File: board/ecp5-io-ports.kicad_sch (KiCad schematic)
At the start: 9 parts

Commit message: Complete schematic
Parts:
- FPGA1: value LFE5UM-381 -> LFE5U-25F; symbol FPGA_Lattice:LFE5UM-85F-6BG381x -> FPGA_Lattice:LFE5U-85F-8BG381x; JLC (none) -> CABGA-381; LCSC (none) -> C1550939
- renumbered C43 to C37, C44 to C38, C45 to C39, C46 to C40, C47 to C41, C48 to C42, C49 to C43, C50 to C44
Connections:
- no-connect marks 127 -> 131
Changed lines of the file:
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@@
 	)
 	(no_connect
+		(at 162.56 120.65)
+	)
+	(no_connect
 		(at 116.84 49.53)
 	)
@@
 	)
 	(no_connect
+		(at 162.56 105.41)
+	)
+	(no_connect
 		(at 67.31 54.61)
 	)
@@
 	)
 	(no_connect
+		(at 162.56 118.11)
+	)
+	(no_connect
 		(at 67.31 80.01)
 	)
@@
 	)
 	(no_connect
+		(at 162.56 113.03)
+	)
+	(no_connect
 		(at 22.86 49.53)
 	)
@@
 		(on_board yes)
 		(dnp no)
-		(property "Reference" "C44"
+		(property "Reference" "C38"
 			(at 65.024 148.082 0)
 			(effects
@@
 			(project "HispalisFPGA"
 				(path "/864346d0-d3ef-428e-a44f-9476f195db98/79b2db60-ab3f-4b1c-9160-e735db7b00f9"
-					(reference "C44")
+					(reference "C38")
 					(unit 1)
 				)
@@
 		(on_board yes)
 		(dnp no)
-		(property "Reference" "C49"
+		(property "Reference" "C43"
 			(at 183.134 35.052 0)
 			(effects
@@
 			(project "HispalisFPGA"
 				(path "/864346d0-d3ef-428e-a44f-9476f195db98/79b2db60-ab3f-4b1c-9160-e735db7b00f9"
-					(reference "C49")
+					(reference "C43")
 					(unit 1)
 				)
@@
 	)
 	(symbol
-		(lib_id "FPGA_Lattice:LFE5UM-85F-6BG381x")
+		(lib_id "FPGA_Lattice:LFE5U-85F-8BG381x")
 		(at 77.47 82.55 0)
 		(unit 3)
@@
 			)
 		)
-		(property "Value" "LFE5UM-381"
+		(property "Value" "LFE5U-25F"
 			(at 83.82 83.8199 0)
 			(effects
@@
 			)
 		)
-		(property "Description" "ECP5 FPGA, 84K LUTs, 1.2V, 3.2Gbps SERDES, BGA-381"
+		(property "Description" "ECP5 FPGA, 84K LUTs, 1.2V, BGA-381"
+			(at 77.47 82.55 0)
+			(effects
+				(font
+					(size 1.27 1.27)
+				)
+				(hide yes)
+			)
+		)
+		(property "JLC" "CABGA-381"
+			(at 77.47 82.55 0)
+			(effects
+				(font
+					(size 1.27 1.27)
+				)
+				(hide yes)
+			)
+		)
+		(property "LCSC" "C1550939"
 			(at 77.47 82.55 0)
 			(effects
@@
 	)
 	(symbol
-		(lib_id "FPGA_Lattice:LFE5UM-85F-6BG381x")
+		(lib_id "FPGA_Lattice:LFE5U-85F-8BG381x")
 		(at 92.71 193.04 0)
 		(unit 7)
@@
 			)
 		)
-		(property "Value" "LFE5UM-381"
+		(property "Value" "LFE5U-25F"
 			(at 99.06 194.3099 0)
 			(effects
@@
 			)
 		)
-		(property "Description" "ECP5 FPGA, 84K LUTs, 1.2V, 3.2Gbps SERDES, BGA-381"
+		(property "Description" "ECP5 FPGA, 84K LUTs, 1.2V, BGA-381"
+			(at 92.71 193.04 0)
+			(effects
+				(font
+					(size 1.27 1.27)
+				)
+				(hide yes)
+			)
+		)
+		(property "JLC" "CABGA-381"
+			(at 92.71 193.04 0)
+			(effects
+				(font
+					(size 1.27 1.27)
+				)
+				(hide yes)
+			)
+		)
+		(property "LCSC" "C1550939"
 			(at 92.71 193.04 0)
 			(effects
@@
 	)
 	(symbol
-		(lib_id "FPGA_Lattice:LFE5UM-85F-6BG381x")
+		(lib_id "FPGA_Lattice:LFE5U-85F-8BG381x")
 		(at 46.99 195.58 0)
 		(unit 6)
@@
 			)
 		)
-		(property "Value" "LFE5UM-381"
+		(property "Value" "LFE5U-25F"
 			(at 53.34 196.8499 0)
 			(effects
@@
 			)
 		)
-		(property "Description" "ECP5 FPGA, 84K LUTs, 1.2V, 3.2Gbps SERDES, BGA-381"
+		(property "Description" "ECP5 FPGA, 84K LUTs, 1.2V, BGA-381"
+			(at 46.99 195.58 0)
+			(effects
+				(font
+					(size 1.27 1.27)
+				)
+				(hide yes)
+			)
+		)
+		(property "JLC" "CABGA-381"
+			(at 46.99 195.58 0)
+			(effects
+				(font
+					(size 1.27 1.27)
+				)
+				(hide yes)
+			)
+		)
+		(property "LCSC" "C1550939"
 			(at 46.99 195.58 0)
 			(effects
@@
 		(on_board yes)
 		(dnp no)
-		(property "Reference" "C43"
+		(property "Reference" "C37"
 			(at 57.404 148.082 0)
 			(effects
@@
 			(project "HispalisFPGA"
 				(path "/864346d0-d3ef-428e-a44f-9476f195db98/79b2db60-ab3f-4b1c-9160-e735db7b00f9"
-					(reference "C43")
+					(reference "C37")
 					(unit 1)
 				)
@@
 	)
 	(symbol
-		(lib_id "FPGA_Lattice:LFE5UM-85F-6BG381x")
+		(lib_id "FPGA_Lattice:LFE5U-85F-8BG381x")
 		(at 127 82.55 0)
 		(unit 4)
@@
 			)
 		)
-		(property "Value" "LFE5UM-381"
+		(property "Value" "LFE5U-25F"
 			(at 133.35 83.8199 0)
 			(effects
@@
 			)
 		)
-		(property "Description" "ECP5 FPGA, 84K LUTs, 1.2V, 3.2Gbps SERDES, BGA-381"
+		(property "Description" "ECP5 FPGA, 84K LUTs, 1.2V, BGA-381"
+			(at 127 82.55 0)
+			(effects
+				(font
+					(size 1.27 1.27)
+				)
+				(hide yes)
+			)
+		)
+		(property "JLC" "CABGA-381"
+			(at 127 82.55 0)
+			(effects
+				(font
+					(size 1.27 1.27)
+				)
+				(hide yes)
+			)
+		)
+		(property "LCSC" "C1550939"
 			(at 127 82.55 0)
 			(effects
@@
 		(on_board yes)
 		(dnp no)
-		(property "Reference" "C46"
+		(property "Reference" "C40"
 			(at 110.744 148.082 0)
 			(effects
@@
 			(project "HispalisFPGA"
 				(path "/864346d0-d3ef-428e-a44f-9476f195db98/79b2db60-ab3f-4b1c-9160-e735db7b00f9"
-					(reference "C46")
+					(reference "C40")
 					(unit 1)
 				)
@@
 		(on_board yes)
 		(dnp no)
-		(property "Reference" "C47"
+		(property "Reference" "C41"
 			(at 153.924 148.082 0)
 			(effects
@@
 			(project "HispalisFPGA"
 				(path "/864346d0-d3ef-428e-a44f-9476f195db98/79b2db60-ab3f-4b1c-9160-e735db7b00f9"
-					(reference "C47")
+					(reference "C41")
 					(unit 1)
 				)
@@
 		(on_board yes)
 		(dnp no)
-		(property "Reference" "C48"
+		(property "Reference" "C42"
 			(at 161.544 148.082 0)
 			(effects
@@
 			(project "HispalisFPGA"
 				(path "/864346d0-d3ef-428e-a44f-9476f195db98/79b2db60-ab3f-4b1c-9160-e735db7b00f9"
-					(reference "C48")
+					(reference "C42")
 					(unit 1)
 				)
@@
 		(on_board yes)
 		(dnp no)
-		(property "Reference" "C45"
+		(property "Reference" "C39"
 			(at 103.124 148.082 0)
 			(effects
@@
 			(project "HispalisFPGA"
 				(path "/864346d0-d3ef-428e-a44f-9476f195db98/79b2db60-ab3f-4b1c-9160-e735db7b00f9"
-					(reference "C45")
+					(reference "C39")
 					(unit 1)
 				)
@@
 	)
 	(symbol
-		(lib_id "FPGA_Lattice:LFE5UM-85F-6BG381x")
+		(lib_id "FPGA_Lattice:LFE5U-85F-8BG381x")
 		(at 33.02 74.93 0)
 		(unit 2)
@@
 			)
 		)
-		(property "Value" "LFE5UM-381"
+		(property "Value" "LFE5U-25F"
 			(at 39.37 76.1999 0)
 			(effects
@@
 			)
 		)
-		(property "Description" "ECP5 FPGA, 84K LUTs, 1.2V, 3.2Gbps SERDES, BGA-381"
+		(property "Description" "ECP5 FPGA, 84K LUTs, 1.2V, BGA-381"
+			(at 33.02 74.93 0)
+			(effects
+				(font
+					(size 1.27 1.27)
+				)
+				(hide yes)
+			)
+		)
+		(property "JLC" "CABGA-381"
+			(at 33.02 74.93 0)
+			(effects
+				(font
+					(size 1.27 1.27)
+				)
+				(hide yes)
+			)
+		)
+		(property "LCSC" "C1550939"
 			(at 33.02 74.93 0)
 			(effects
@@
 	)
 	(symbol
-		(lib_id "FPGA_Lattice:LFE5UM-85F-6BG381x")
+		(lib_id "FPGA_Lattice:LFE5U-85F-8BG381x")
 		(at 172.72 82.55 0)
 		(unit 5)
@@
 			)
 		)
-		(property "Value" "LFE5UM-381"
+		(property "Value" "LFE5U-25F"
 			(at 179.07 83.8199 0)
 			(effects
@@
 			)
 		)
-		(property "Description" "ECP5 FPGA, 84K LUTs, 1.2V, 3.2Gbps SERDES, BGA-381"
+		(property "Description" "ECP5 FPGA, 84K LUTs, 1.2V, BGA-381"
+			(at 172.72 82.55 0)
+			(effects
+				(font
+					(size 1.27 1.27)
+				)
+				(hide yes)
+			)
+		)
+		(property "JLC" "CABGA-381"
+			(at 172.72 82.55 0)
+			(effects
+				(font
+					(size 1.27 1.27)
+				)
+				(hide yes)
+			)
+		)
+		(property "LCSC" "C1550939"
 			(at 172.72 82.55 0)
 			(effects
@@
 	)
 	(symbol
-		(lib_id "FPGA_Lattice:LFE5UM-85F-6BG381x")
+		(lib_id "FPGA_Lattice:LFE5U-85F-8BG381x")
 		(at 143.51 170.18 0)
 		(unit 8)
@@
 			)
 		)
-		(property "Value" "LFE5UM-381"
+		(property "Value" "LFE5U-25F"
 			(at 149.86 171.4499 0)
 			(effects
@@
 			)
 		)
-		(property "Description" "ECP5 FPGA, 84K LUTs, 1.2V, 3.2Gbps SERDES, BGA-381"
+		(property "Description" "ECP5 FPGA, 84K LUTs, 1.2V, BGA-381"
+			(at 143.51 170.18 0)
+			(effects
+				(font
+					(size 1.27 1.27)
+				)
+				(hide yes)
+			)
+		)
+		(property "JLC" "CABGA-381"
+			(at 143.51 170.18 0)
+			(effects
+				(font
+					(size 1.27 1.27)
+				)
+				(hide yes)
+			)
+		)
+		(property "LCSC" "C1550939"
 			(at 143.51 170.18 0)
 			(effects
@@
 		(on_board yes)
 		(dnp no)
-		(property "Reference" "C50"
+		(property "Reference" "C44"
 			(at 190.754 35.052 0)
 			(effects
@@
 			(project "HispalisFPGA"
 				(path "/864346d0-d3ef-428e-a44f-9476f195db98/79b2db60-ab3f-4b1c-9160-e735db7b00f9"
-					(reference "C50")
+					(reference "C44")
 					(unit 1)
 				)

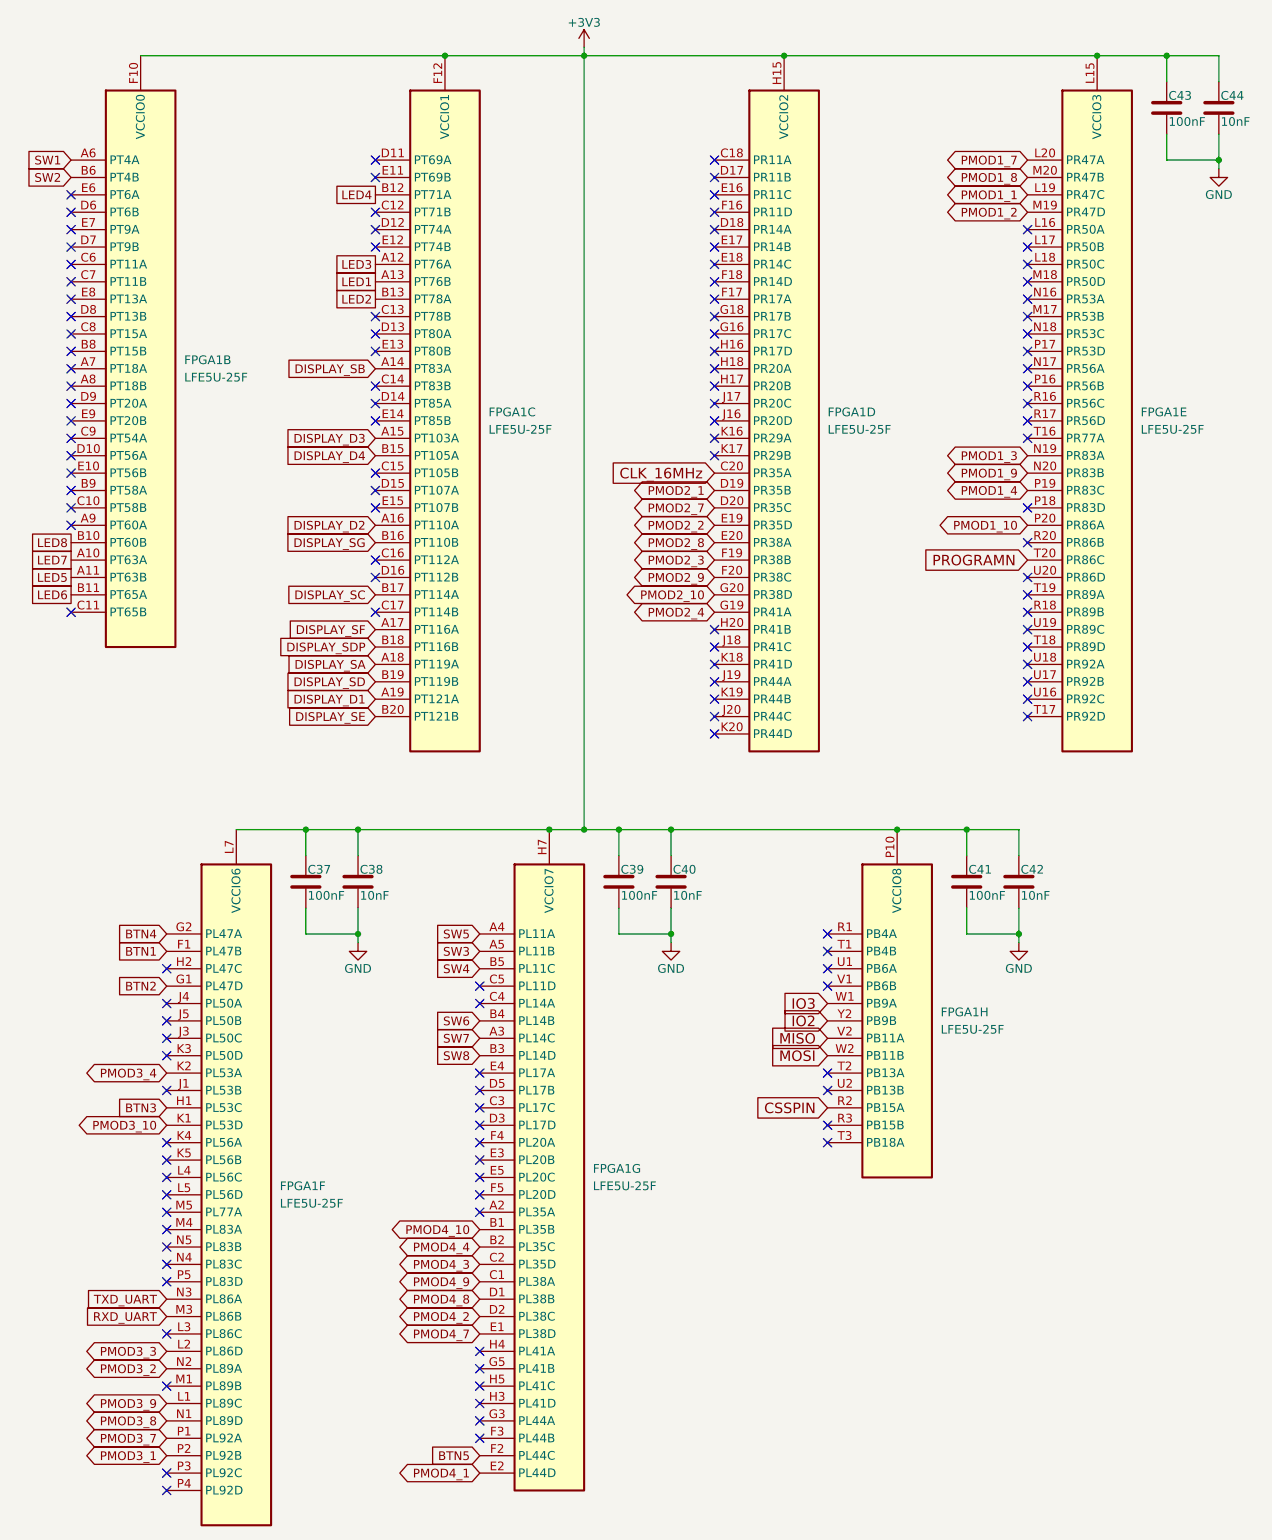
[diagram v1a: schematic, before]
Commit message: Finish routing and remove unneeded silkscreen
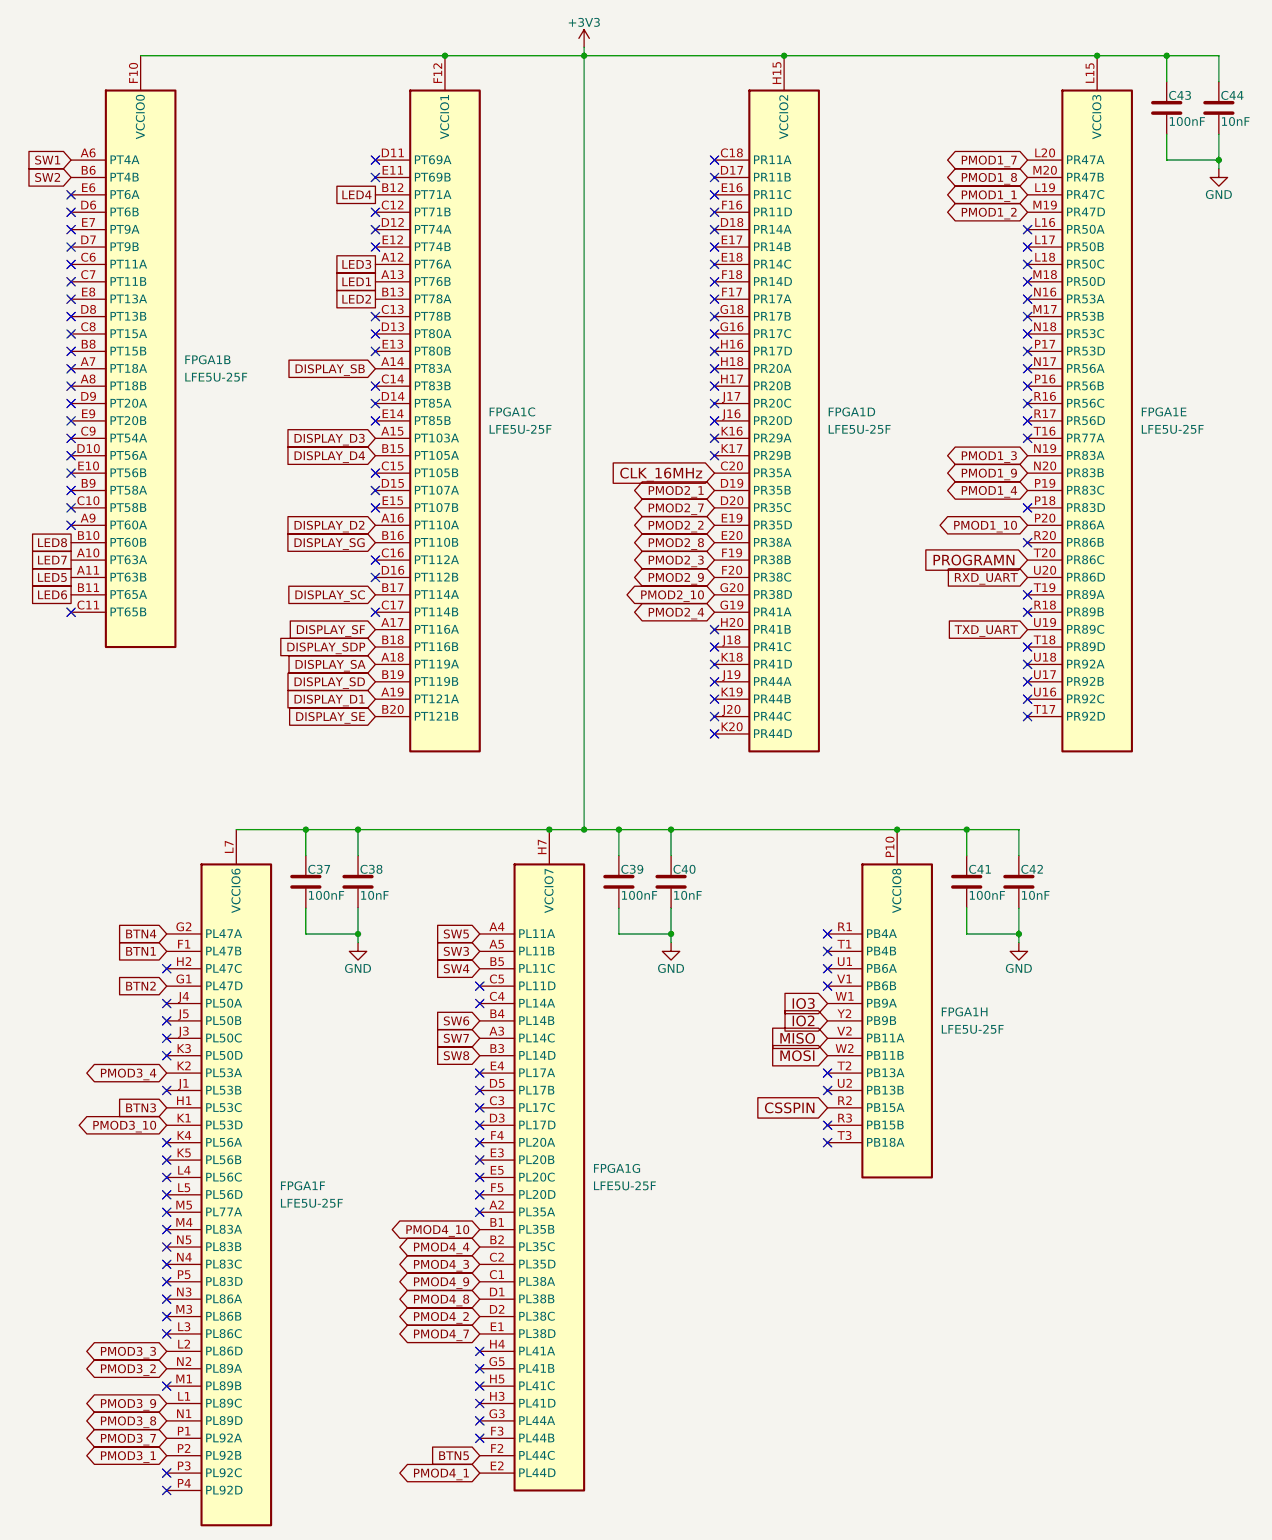
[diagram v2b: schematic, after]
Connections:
- net RXD_UART: now also FPGA1.U20 (PR86D); no longer FPGA1.M3 (PL86B)
- net TXD_UART: now also FPGA1.U19 (PR89C); no longer FPGA1.N3 (PL86A)
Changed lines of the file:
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@@
+	)
+	(no_connect
+		(at 36.83 213.36)
 	)
 	(no_connect
@@
 	)
 	(no_connect
-		(at 162.56 105.41)
-	)
-	(no_connect
 		(at 67.31 54.61)
 	)
@@
 	)
 	(no_connect
-		(at 162.56 113.03)
-	)
-	(no_connect
 		(at 22.86 49.53)
 	)
@@
 	(no_connect
 		(at 116.84 77.47)
+	)
+	(no_connect
+		(at 36.83 210.82)
 	)
 	(wire
@@
 		)
 	)
-	(global_label "RXD_UART"
-		(shape input)
-		(at 36.83 213.36 180)
-		(fields_autoplaced yes)
-		(effects
-			(font
-				(size 1.27 1.27)
-			)
-			(justify right)
-		)
-		(property "Intersheetrefs" "${INTERSHEET_REFS}"
-			(at 25.1252 213.36 0)
-			(effects
-				(font
-					(size 1.27 1.27)
-				)
-				(justify right)
-				(hide yes)
-			)
-		)
-	)
 	(global_label "IO2"
 		(shape input)
@@
 		)
 	)
-	(global_label "TXD_UART"
+	(global_label "RXD_UART"
 		(shape input)
-		(at 36.83 210.82 180)
+		(at 162.56 105.41 180)
 		(fields_autoplaced yes)
 		(effects
@@
 		)
 		(property "Intersheetrefs" "${INTERSHEET_REFS}"
-			(at 25.4276 210.82 0)
+			(at 150.8552 105.41 0)
 			(effects
 				(font
@@
 				(hide yes)
 			)
+		)
+	)
+	(global_label "TXD_UART"
+		(shape input)
+		(at 162.56 113.03 180)
+		(fields_autoplaced yes)
+		(effects
+			(font
+				(size 1.27 1.27)
+			)
+			(justify right)
+		)
+		(property "Intersheetrefs" "${INTERSHEET_REFS}"
+			(at 151.1576 113.03 0)
+			(effects
+				(font
+					(size 1.27 1.27)
+				)
+				(justify right)
+				(hide yes)
+			)
